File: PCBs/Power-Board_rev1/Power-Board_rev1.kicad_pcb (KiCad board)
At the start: 2 copper layers, 8 parts, among them J1 Conn_01x04, Q1 RT6150AGQW

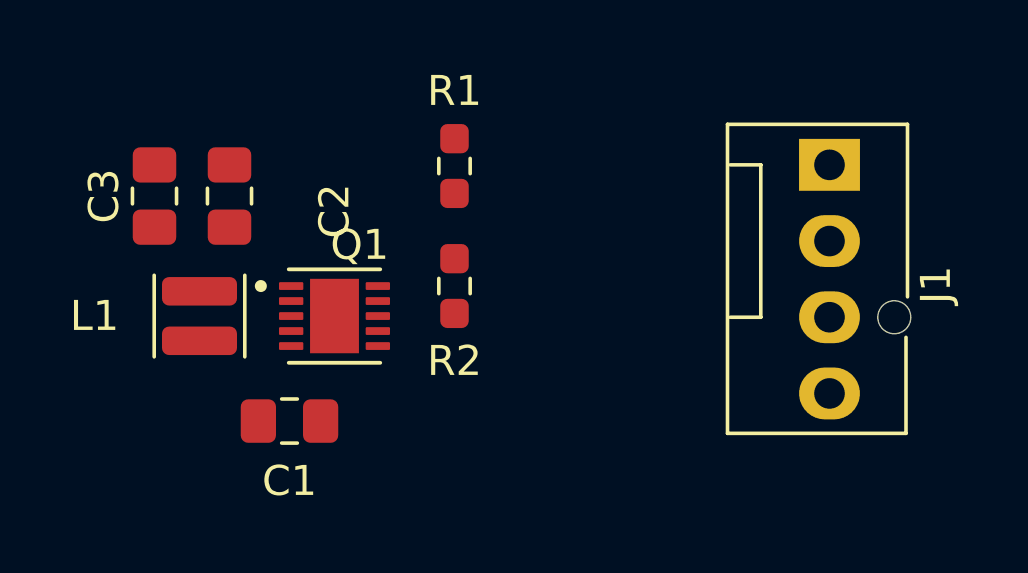
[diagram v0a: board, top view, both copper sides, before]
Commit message: updated power board layout, added extra pads for additional capacitors
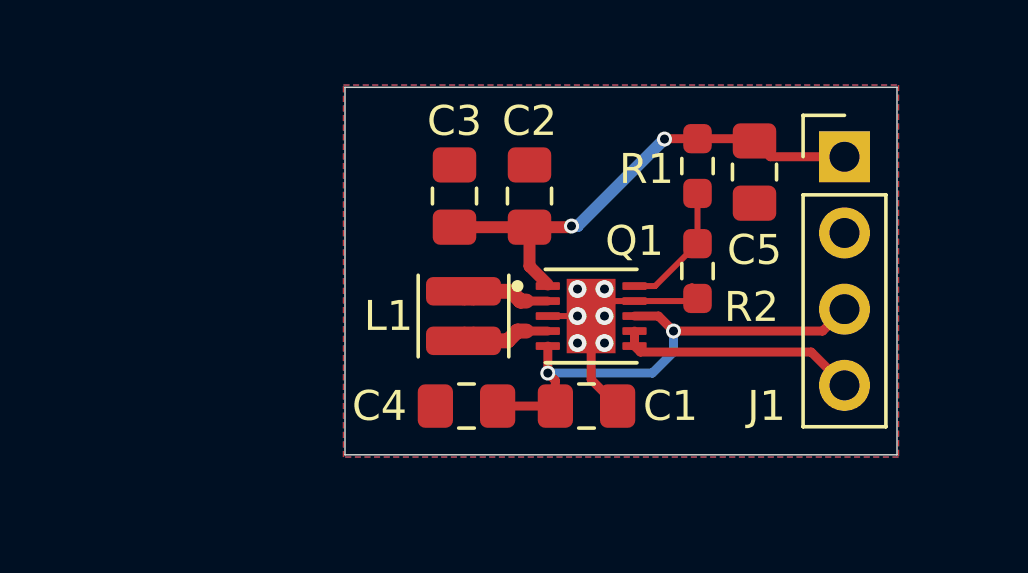
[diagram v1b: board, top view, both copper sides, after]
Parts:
- added C4: 10uF, Capacitor_SMD:C_0805_2012Metric_Pad1.18x1.45mm_HandSolder, F.Cu at (154.4, 104.5)
- added C5: 10uF, Capacitor_SMD:C_0805_2012Metric_Pad1.18x1.45mm_HandSolder, F.Cu at (164.0, 96.7)
- J1: footprint Connector:FanPinHeader_1x04_P2.54mm_Vertical -> Connector_PinHeader_2.54mm:PinHeader_1x04_P2.54mm_Vertical
- moved C2 10.0 mm to (156.5, 97.5)
- moved C3 10.0 mm to (154.0, 97.5)
- moved C1 9.91 mm to (158.4, 104.5)
- moved L1 8.80 mm to (154.3, 101.5)
- moved Q1 8.56 mm to (158.6, 101.5)
- moved R2 8.12 mm to (162.1, 100.0)
- moved R1 8.10 mm to (162.1, 96.5), turned to -90 degrees
- moved J1 0.57 mm to (167.0, 96.2), turned to 0 degrees
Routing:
- net /VOUT: track 0.00 -> 17.5 mm, vias 0 -> 2
- net /VIN: track 0.00 -> 16.9 mm, vias 0 -> 2
- net GND: track 0.00 -> 8.72 mm, vias 0 -> 6
- net /EN: track 0.00 -> 8.04 mm
- net Net-(Q1-FB): track 0.00 -> 4.36 mm
- net Net-(Q1-LX2): track 0.00 -> 3.86 mm
- net Net-(Q1-LX1): track 0.00 -> 3.86 mm
- added copper zone on B.Cu, net GND
- added copper zone on F.Cu, net GND
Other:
- board outline added: 18.4 x 12.2 mm

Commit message: Power board layout rev-1 mostly finished
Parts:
- J1: footprint Connector_PinHeader_2.54mm:PinHeader_1x04_P2.54mm_Vertical -> Header:PinHeader_1x04_P2.54mm_Vertical_GND2
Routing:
- net GND: track 8.72 -> 13.7 mm
- net /VOUT: track 17.5 -> 16.9 mm
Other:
- board text added: "EN"
- board text added: "GND"
- board text added: "VIN"
- board text added: "VOUT"
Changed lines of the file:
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@@
 			(outputformat 1)
 			(mirror no)
-			(drillshape 1)
+			(drillshape 0)
 			(scaleselection 1)
-			(outputdirectory "")
+			(outputdirectory "Gerber/")
 		)
 	)
@@
 			)
 		)
-		(property "JLCPCB Part#" "C531341"
+		(property "JLCPCB Part#" "C95841"
 			(at 0 0 90)
 			(unlocked yes)
@@
 			)
 		)
-		(property "JLCPCB Part#" "C531341"
+		(property "JLCPCB Part#" "C95841"
 			(at 0 0 90)
 			(unlocked yes)
@@
 			)
 		)
-		(property "JLCPCB Part#" ""
+		(property "JLCPCB Part#" "C5832372"
 			(at 0 0 90)
 			(unlocked yes)
@@
 			)
 		)
-		(property "JLCPCB Part#" "C531341"
+		(property "JLCPCB Part#" "C95841"
 			(at 0 0 270)
 			(unlocked yes)
@@
 		(embedded_fonts no)
 	)
-	(footprint "Connector_PinHeader_2.54mm:PinHeader_1x04_P2.54mm_Vertical"
+	(footprint "Header:PinHeader_1x04_P2.54mm_Vertical_GND2"
 		(layer "F.Cu")
 		(at 167 96.19)
@@
 		(tags "Through hole pin header THT 1x04 2.54mm single row")
 		(property "Reference" "J1"
-			(at -2.6 8.31 0)
+			(at -2.7 8.71 0)
 			(layer "F.SilkS")
 			(effects
@@
 			)
 		)
-		(pad "1" thru_hole rect
+		(pad "1" thru_hole circle
 			(at 0 0)
 			(size 1.7 1.7)
@@
 			(pintype "passive")
 		)
-		(pad "2" thru_hole circle
+		(pad "2" thru_hole rect
 			(at 0 2.54)
 			(size 1.7 1.7)
@@
 		(layer "Edge.Cuts")
 	)
+	(gr_text "VIN"
+		(at 163.1 100.7 180)
+		(layer "B.SilkS")
+		(effects
+			(font
+				(size 1 1)
+				(thickness 0.1)
+			)
+			(justify left bottom mirror)
+		)
+	)
+	(gr_text "EN"
+		(at 163.3 103.4 180)
+		(layer "B.SilkS")
+		(effects
+			(font
+				(size 1 1)
+				(thickness 0.1)
+			)
+			(justify left bottom mirror)
+		)
+	)
+	(gr_text "GND"
+		(at 162.5 98.2 180)
+		(layer "B.SilkS")
+		(effects
+			(font
+				(size 1 1)
+				(thickness 0.1)
+			)
+			(justify left bottom mirror)
+		)
+	)
+	(gr_text "VOUT"
+		(at 161.6 95.5 180)
+		(layer "B.SilkS")
+		(effects
+			(font
+				(size 1 1)
+				(thickness 0.1)
+			)
+			(justify left bottom mirror)
+		)
+	)
 	(segment
 		(start 160 101.5)
@@
 	)
 	(segment
-		(start 166.27 102)
-		(end 167 101.27)
+		(start 167 101.28)
+		(end 166.99 101.28)
 		(width 0.3)
 		(layer "F.Cu")
@@
 	)
 	(segment
+		(start 167 101.27)
+		(end 166.27 102)
+		(width 0.3)
+		(layer "F.Cu")
+		(net 1)
+	)
+	(segment
 		(start 161.3 102)
 		(end 166.27 102)
@@
 	)
 	(segment
+		(start 160.4115 105.474)
+		(end 160.6 105.474)
+		(width 0.3)
+		(layer "F.Cu")
+		(net 2)
+	)
+	(segment
+		(start 159.4375 104.5)
+		(end 160.4115 105.474)
+		(width 0.3)
+		(layer "F.Cu")
+		(net 2)
+	)
+	(segment
+		(start 153.3625 104.5)
+		(end 153.3625 104.3625)
+		(width 0.3)
+		(layer "F.Cu")
+		(net 2)
+	)
+	(segment
+		(start 153.3625 104.3625)
+		(end 152.4 103.4)
+		(width 0.3)
+		(layer "F.Cu")
+		(net 2)
+	)
+	(segment
+		(start 167 98.9)
+		(end 165.8 100.1)
+		(width 0.3)
+		(layer "F.Cu")
+		(net 2)
+	)
+	(segment
+		(start 159.4375 104.5)
+		(end 159.5 104.5)
+		(width 0.3)
+		(layer "F.Cu")
+		(net 2)
+	)
+	(segment
 		(start 160 101)
 		(end 162.0125 101)
@@
 	)
 	(segment
+		(start 160.6 105.474)
+		(end 160.626 105.474)
+		(width 0.3)
+		(layer "F.Cu")
+		(net 2)
+	)
+	(segment
 		(start 159.055 101)
 		(end 158.555 101.5)
@@
 	)
 	(segment
+		(start 167 98.73)
+		(end 167 98.9)
+		(width 0.3)
+		(layer "F.Cu")
+		(net 2)
+	)
+	(segment
 		(start 158.555 102.5)
 		(end 158.555 101.5)
@@
 	)
 	(via
-		(at 159 102.4)
+		(at 158.95 102.3)
 		(size 0.6)
 		(drill 0.3)
 		(layers "F.Cu" "B.Cu")
+		(tenting none)
 		(net 2)
 	)
 	(via
-		(at 159 101.5)
+		(at 158.95 101.5)
 		(size 0.6)
 		(drill 0.3)
 		(layers "F.Cu" "B.Cu")
+		(tenting none)
 		(net 2)
 	)
 	(via
-		(at 158.1 100.6)
+		(at 158.15 100.7)
 		(size 0.6)
 		(drill 0.3)
 		(layers "F.Cu" "B.Cu")
+		(tenting none)
 		(net 2)
 	)
 	(via
-		(at 158.1 101.5)
+		(at 158.15 101.5)
 		(size 0.6)
 		(drill 0.3)
 		(layers "F.Cu" "B.Cu")
+		(tenting none)
 		(net 2)
 	)
 	(via
-		(at 159 100.6)
+		(at 158.95 100.7)
 		(size 0.6)
 		(drill 0.3)
 		(layers "F.Cu" "B.Cu")
+		(tenting none)
 		(net 2)
 	)
 	(via
-		(at 158.1 102.4)
+		(at 158.15 102.3)
 		(size 0.6)
 		(drill 0.3)
 		(layers "F.Cu" "B.Cu")
+		(tenting none)
 		(net 2)
 	)
@@
 	)
 	(segment
-		(start 167 96.19)
-		(end 164.5275 96.19)
-		(width 0.3)
-		(layer "F.Cu")
-		(net 3)
-	)
-	(segment
 		(start 156.5 99.839)
 		(end 157.11 100.449)
@@
 	)
 	(segment
-		(start 164.5275 96.19)
-		(end 164 95.6625)
-		(width 0.3)
-		(layer "F.Cu")
-		(net 3)
-	)
-	(segment
 		(start 156.5 98.5375)
 		(end 156.5 98.5)
@@
 	)
 	(segment
+		(start 164 95.6625)
+		(end 164.2625 95.6625)
+		(width 0.3)
+		(layer "F.Cu")
+		(net 3)
+	)
+	(segment
 		(start 163.925 95.5875)
 		(end 164 95.6625)
@@
 	)
 	(segment
+		(start 167 96.19)
+		(end 164.5275 96.19)
+		(width 0.3)
+		(layer "F.Cu")
+		(net 3)
+	)
+	(segment
 		(start 157.8625 98.5375)
 		(end 157.9 98.5)
@@
 	)
 	(segment
-		(start 162.1 95.5875)
-		(end 161.0125 95.5875)
+		(start 164.5275 96.19)
+		(end 164 95.6625)
 		(width 0.3)
 		(layer "F.Cu")
@@
 	)
 	(segment
-		(start 166.3975 95.5875)
-		(end 167 96.19)
+		(start 162.1 95.5875)
+		(end 161.0125 95.5875)
 		(width 0.3)
 		(layer "F.Cu")
@@
 	)
 	(segment
-		(start 160.2 102.7)
-		(end 165.89 102.7)
+		(start 165.9 102.71)
+		(end 165.89 102.71)
 		(width 0.3)
 		(layer "F.Cu")
@@
 	)
 	(segment
-		(start 160 102)
-		(end 160 102.5)
+		(start 165.89 102.7)
+		(end 165.89 102.71)
 		(width 0.3)
 		(layer "F.Cu")
@@
 	)
 	(segment
-		(start 165.89 102.7)
-		(end 167 103.81)
+		(start 167 103.81)
+		(end 165.9 102.71)
+		(width 0.3)
+		(layer "F.Cu")
+		(net 4)
+	)
+	(segment
+		(start 160.2 102.7)
+		(end 165.89 102.7)
+		(width 0.3)
+		(layer "F.Cu")
+		(net 4)
+	)
+	(segment
+		(start 160 102)
+		(end 160 102.5)
 		(width 0.3)
 		(layer "F.Cu")

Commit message: Updated power board files
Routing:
- net GND: track 13.7 -> 18.5 mm
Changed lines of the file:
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@@
-	)
-	(segment
-		(start 162 100.5875)
-		(end 161.9125 100.5)
-		(width 0.2)
-		(layer "F.Cu")
-		(net 2)
 	)
 	(segment
@@
 	)
 	(segment
+		(start 152.3885 105.474)
+		(end 152.2 105.474)
+		(width 0.3)
+		(layer "F.Cu")
+		(net 2)
+	)
+	(segment
+		(start 167 98.7)
+		(end 165.7 97.4)
+		(width 0.3)
+		(layer "F.Cu")
+		(net 2)
+	)
+	(segment
 		(start 167 98.9)
 		(end 165.8 100.1)
@@
 	)
 	(segment
+		(start 153.3625 104.5)
+		(end 152.3885 105.474)
+		(width 0.3)
+		(layer "F.Cu")
+		(net 2)
+	)
+	(segment
 		(start 159.4375 104.5)
 		(end 158.555 103.6175)
@@
 		(layer "F.Cu")
 		(net 2)
+	)
+	(segment
+		(start 159.5 104.5)
+		(end 160.5 103.5)
+		(width 0.3)
+		(layer "F.Cu")
+		(net 2)
+	)
+	(segment
+		(start 167 98.73)
+		(end 167 98.7)
+		(width 0.3)
+		(layer "F.Cu")
+		(net 2)

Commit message: Made Power Board 4 Layers
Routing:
- added copper zone on In1.Cu, net GND
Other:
- copper layers 2 -> 4
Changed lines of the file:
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@@
 	(layers
 		(0 "F.Cu" signal)
+		(4 "In1.Cu" signal)
+		(6 "In2.Cu" signal)
 		(2 "B.Cu" signal)
 		(9 "F.Adhes" user "F.Adhesive")
@@
 			)
 			(layer "dielectric 1"
+				(type "prepreg")
+				(thickness 0.1)
+				(material "FR4")
+				(epsilon_r 4.5)
+				(loss_tangent 0.02)
+			)
+			(layer "In1.Cu"
+				(type "copper")
+				(thickness 0.035)
+			)
+			(layer "dielectric 2"
 				(type "core")
-				(thickness 1.51)
+				(thickness 1.24)
+				(material "FR4")
+				(epsilon_r 4.5)
+				(loss_tangent 0.02)
+			)
+			(layer "In2.Cu"
+				(type "copper")
+				(thickness 0.035)
+			)
+			(layer "dielectric 3"
+				(type "prepreg")
+				(thickness 0.1)
 				(material "FR4")
 				(epsilon_r 4.5)
@@
 		(net 2)
 		(net_name "GND")
-		(layers "F.Cu" "B.Cu")
+		(layers "F.Cu" "B.Cu" "In1.Cu")
 		(hatch edge 0.5)
 		(connect_pads

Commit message: restructured main layout, needs some cleanup still
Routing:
- removed copper zone on In1.Cu, net GND
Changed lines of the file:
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@@
 		(net 2)
 		(net_name "GND")
-		(layers "F.Cu" "B.Cu" "In1.Cu")
+		(layers "F.Cu" "B.Cu")
 		(hatch edge 0.5)
 		(connect_pads
